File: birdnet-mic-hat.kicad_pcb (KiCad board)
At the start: 4 copper layers, 17.8 x 22.7 mm, 26 parts, among them J1 PJ-327A0-SMT, J3 DF40HC(3.5)-30DS-0.4V(51), Q1 MMBT3904, U1 TLV320ADC5140, U2 TPS7A2033PDBVR

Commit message: Remove manually placed C12 and J1 silkscreen labels
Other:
- board text removed: "C12"
- board text removed: "J1"

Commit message: Remove remaining MIC and MIC HAT silkscreen text
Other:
- board text removed: "MIC"
- board text removed: "MIC HAT"
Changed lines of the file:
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@@
 		(layer "Edge.Cuts")
-	)
-	(gr_text "MIC"
-		(at 102.3 107.98 0)
-		(layer "F.SilkS")
-		(effects
-			(font
-				(size 0.8 0.8)
-				(thickness 0.12)
-			)
-		)
-	)
-	(gr_text "MIC HAT"
-		(at 100.8 125.4 90)
-		(layer "F.SilkS")
-		(effects
-			(font
-				(size 0.8 0.8)
-				(thickness 0.12)
-			)
-		)
 	)
 	(segment

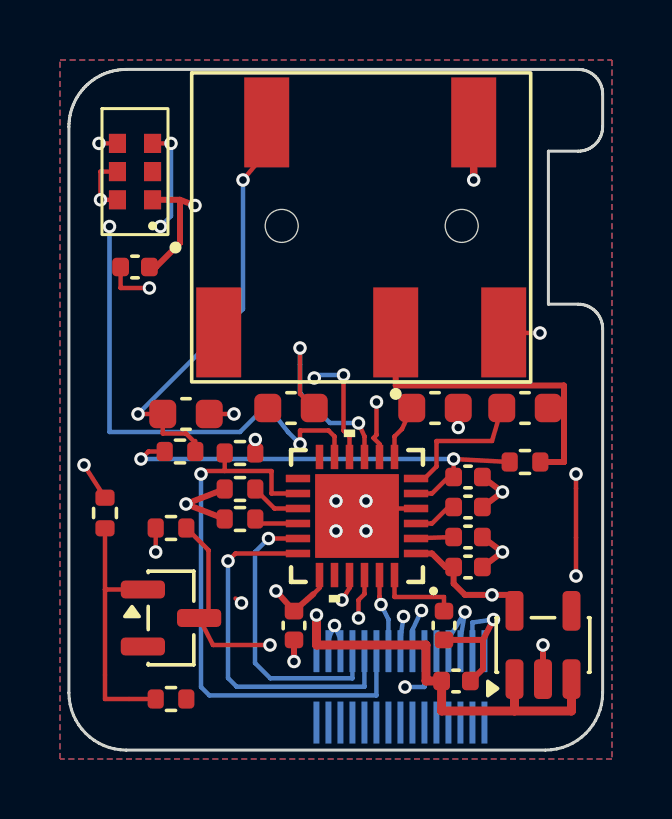
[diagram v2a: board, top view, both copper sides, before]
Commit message: Save manual routing refinements before trace cleanup
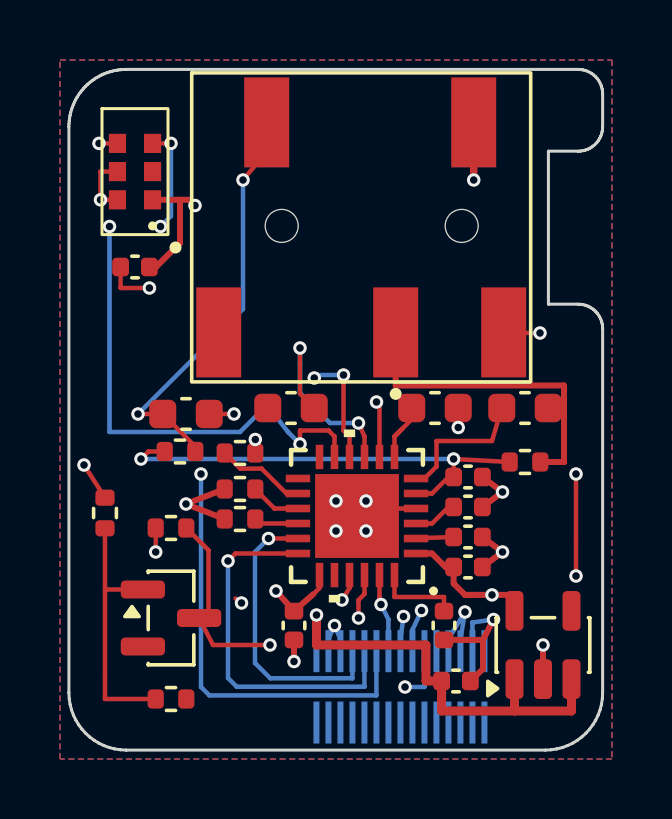
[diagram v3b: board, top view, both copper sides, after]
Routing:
- net /ADC_RST: track 18.7 -> 17.4 mm
- net /JACK_RING: track 13.1 -> 12.6 mm
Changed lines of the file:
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@@
-	)
-	(segment
-		(start 104 119.35)
-		(end 104.31 119.66)
-		(width 0.15)
-		(layer "F.Cu")
-		(net "/JACK_RING")
 	)
 	(segment
 		(start 104.31 119.95)
-		(end 104.31 119.6)
+		(end 104.31 119.785)
 		(width 0.15)
 		(layer "F.Cu")
@@
 	(segment
 		(start 103.225 118.7)
-		(end 103.225 119.35)
+		(end 102.4 118.7)
 		(width 0.15)
 		(layer "F.Cu")
@@
 	)
 	(segment
-		(start 103.225 118.7)
-		(end 102.4 118.7)
-		(width 0.15)
-		(layer "F.Cu")
-		(net "/JACK_RING")
-	)
-	(segment
-		(start 103.225 119.35)
-		(end 104 119.35)
+		(start 104.31 119.785)
+		(end 103.225 118.7)
 		(width 0.15)
 		(layer "F.Cu")
@@
 	)
 	(segment
-		(start 106.85 121.35)
-		(end 106.85 120.6)
+		(start 105.811999 120.522)
+		(end 105.289999 120)
+		(width 0.15)
+		(layer "F.Cu")
+		(net "/ADC_RST")
+	)
+	(segment
+		(start 107.7315 121.349999)
+		(end 107.349999 121.349999)
 		(width 0.15)
 		(layer "F.Cu")
@@
 	)
 	(segment
-		(start 105.29 120.6)
-		(end 105.29 120)
+		(start 106.522 120.522)
+		(end 105.811999 120.522)
 		(width 0.15)
 		(layer "F.Cu")
@@
 	)
 	(segment
-		(start 107.531 121.35)
-		(end 106.85 121.35)
-		(width 0.15)
-		(layer "F.Cu")
-		(net "/ADC_RST")
-	)
-	(segment
-		(start 106.85 120.6)
-		(end 104.6 120.6)
+		(start 107.349999 121.349999)
+		(end 106.522 120.522)
 		(width 0.15)
 		(layer "F.Cu")
@@
 	)
 	(segment
-		(start 103.8 111.56)
-		(end 104.3 111.75)
-		(width 0.2)
-		(layer "F.Cu")
-		(net "AVDD")
-	)
-	(segment
 		(start 103.8 113)
 		(end 103 113.8)
@@
 	)
 	(segment
+		(start 104.11 111.56)
+		(end 104.3 111.75)
+		(width 0.2)
+		(layer "F.Cu")
+		(net "AVDD")
+	)
+	(segment
+		(start 103.8 111.56)
+		(end 104.11 111.56)
+		(width 0.2)
+		(layer "F.Cu")
+		(net "AVDD")
+	)
+	(segment
 		(start 112.2 123.35)
 		(end 112.65 123.8)
@@
 	(segment
 		(start 115.3 113.5)
+		(end 115.3 123.63)
+		(width 0.2)
+		(layer "In2.Cu")
+		(net "AVDD")
+	)
+	(segment
+		(start 115.3 123.63)
+		(end 114.2 124.73)
+		(width 0.2)
+		(layer "In2.Cu")
+		(net "AVDD")
+	)
+	(segment
+		(start 104.3 111.75)
 		(end 104.3 113.5)
 		(width 0.2)
@@
 	)
 	(segment
-		(start 114.2 124.73)
-		(end 115.3 123.63)
-		(width 0.2)
-		(layer "In2.Cu")
-		(net "AVDD")
-	)
-	(segment
-		(start 115.3 123.63)
+		(start 104.3 113.5)
 		(end 115.3 113.5)
-		(width 0.2)
-		(layer "In2.Cu")
-		(net "AVDD")
-	)
-	(segment
-		(start 104.3 113.5)
-		(end 104.3 111.75)
 		(width 0.2)
 		(layer "In2.Cu")
@@
 	)
 	(segment
-		(start 110.35 118.3)
-		(end 110.35 119.4)
+		(start 110.450001 120.1315)
+		(end 110.450001 118.400001)
 		(width 0.15)
 		(layer "F.Cu")
@@
 	)
 	(segment
-		(start 110.25 119.5)
-		(end 110.45 119.7)
-		(width 0.15)
-		(layer "F.Cu")
-		(net "/MIC_RING")
-	)
-	(segment
-		(start 110.35 119.4)
-		(end 110.25 119.5)
-		(width 0.15)
-		(layer "F.Cu")
-		(net "/MIC_RING")
-	)
-	(segment
-		(start 110.45 119.7)
-		(end 110.45 120.1315)
+		(start 110.450001 118.400001)
+		(end 110.35 118.3)
 		(width 0.15)
 		(layer "F.Cu")
@@
 	)
 	(segment
-		(start 111.2 119.2)
-		(end 111.525 118.5)
+		(start 111.524999 118.875001)
+		(end 111.524999 118.5)
 		(width 0.15)
 		(layer "F.Cu")
@@
 		(width 0.15)
 		(layer "F.Cu")
+		(net "/MIC_TIP_N")
+	)
+	(segment
+		(start 110.95 119.45)
+		(end 111.524999 118.875001)
+		(width 0.15)
+		(layer "F.Cu")

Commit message: Clean supply and signal routing and remove redundant via
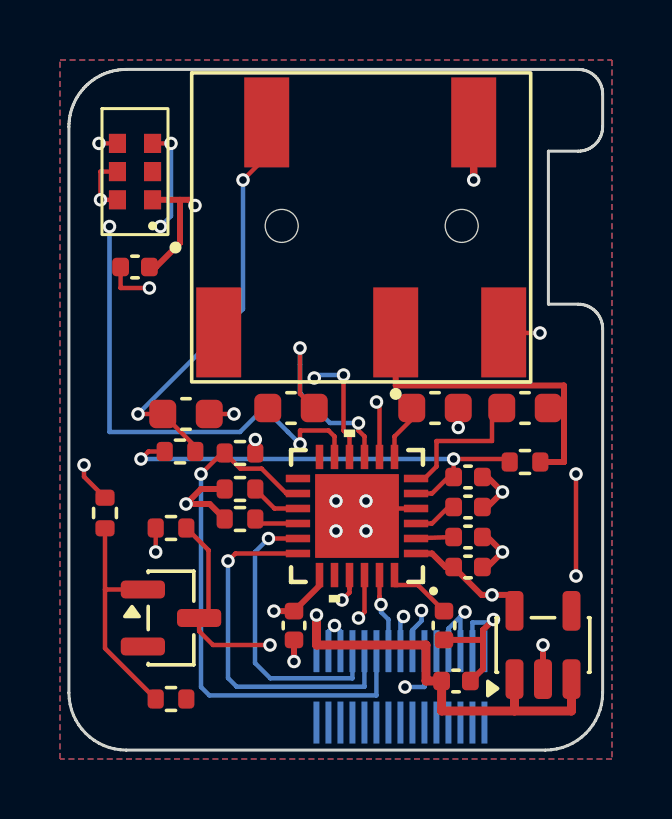
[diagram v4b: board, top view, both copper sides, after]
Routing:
- net AVDD: track 33.6 -> 32.5 mm
- net Net-(Q1-B): track 8.64 -> 7.65 mm
- net /ADC_RST: track 17.4 -> 18.3 mm
- net GND: track 20.9 -> 21.5 mm
- net DREG: track 2.85 -> 2.34 mm
- net VCC_3V3: track 23.5 -> 23.3 mm, vias 5 -> 4

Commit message: Route PDM signals on front copper and remove seven signal vias
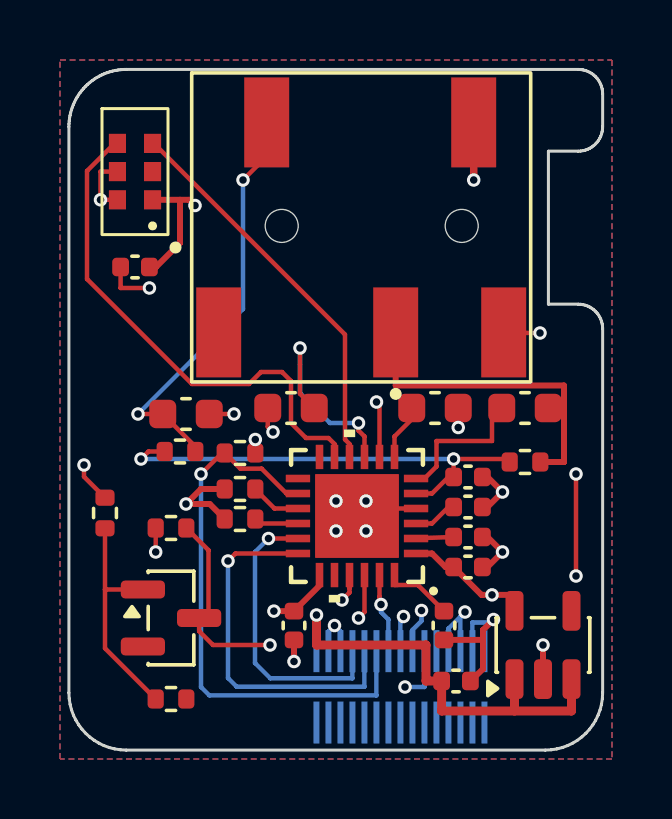
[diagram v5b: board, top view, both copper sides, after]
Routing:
- net /PDM_CLK: track 20.4 -> 17.1 mm, vias 3 -> 0
- net /PDM_DATA: track 16.0 -> 13.2 mm, vias 4 -> 0
- net GND: track 21.5 -> 22.3 mm, vias 15 -> 16
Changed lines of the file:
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@@
+	)
+	(segment
+		(start 106.725 119.125)
+		(end 106.9 119.3)
+		(width 0.15)
+		(layer "F.Cu")
+		(net "GND")
 	)
 	(segment
@@
 	)
 	(segment
+		(start 106.725 118.5)
+		(end 106.725 119.125)
+		(width 0.15)
+		(layer "F.Cu")
+		(net "GND")
+	)
+	(segment
 		(start 113.88 122.8)
 		(end 114.05 122.8)
@@
 	)
 	(via
+		(at 106.9 119.3)
+		(size 0.45)
+		(drill 0.25)
+		(layers "F.Cu" "B.Cu")
+		(net "GND")
+	)
+	(via
 		(at 110 121.6)
 		(size 0.45)
@@
 	)
 	(segment
-		(start 109.25 117.4)
-		(end 109.25 119.25)
+		(start 102.884999 109.68)
+		(end 102.93 109.68)
 		(width 0.15)
 		(layer "F.Cu")
@@
 	)
 	(segment
-		(start 109.45 119.45)
+		(start 109.3 119.55)
+		(end 109.45 119.7)
+		(width 0.15)
+		(layer "F.Cu")
+		(net "/PDM_DATA")
+	)
+	(segment
+		(start 102.93 109.68)
+		(end 109.3 116.05)
+		(width 0.15)
+		(layer "F.Cu")
+		(net "/PDM_DATA")
+	)
+	(segment
+		(start 109.3 116.05)
+		(end 109.3 119.55)
+		(width 0.15)
+		(layer "F.Cu")
+		(net "/PDM_DATA")
+	)
+	(segment
+		(start 109.45 119.7)
 		(end 109.45 120.1315)
 		(width 0.15)
@@
 	)
 	(segment
-		(start 109.25 119.25)
-		(end 109.45 119.45)
-		(width 0.15)
-		(layer "F.Cu")
-		(net "/PDM_DATA")
-	)
-	(segment
-		(start 102.885 109.68)
-		(end 103.5 109.68)
-		(width 0.15)
-		(layer "F.Cu")
-		(net "/PDM_DATA")
-	)
-	(via
-		(at 103.15 112.45)
-		(size 0.45)
-		(drill 0.25)
-		(layers "F.Cu" "B.Cu")
-		(net "/PDM_DATA")
-	)
-	(via
-		(at 108.275 117.5)
-		(size 0.45)
-		(drill 0.25)
-		(layers "F.Cu" "B.Cu")
-		(net "/PDM_DATA")
-	)
-	(via
-		(at 109.25 117.4)
-		(size 0.45)
-		(drill 0.25)
-		(layers "F.Cu" "B.Cu")
-		(net "/PDM_DATA")
-	)
-	(via
-		(at 103.5 109.68)
-		(size 0.45)
-		(drill 0.25)
-		(layers "F.Cu" "B.Cu")
-		(net "/PDM_DATA")
-	)
-	(segment
-		(start 108.375 117.4)
-		(end 109.25 117.4)
-		(width 0.15)
-		(layer "B.Cu")
-		(net "/PDM_DATA")
-	)
-	(segment
-		(start 103.5 109.68)
-		(end 103.5 112.1)
-		(width 0.15)
-		(layer "B.Cu")
-		(net "/PDM_DATA")
-	)
-	(segment
-		(start 103.5 112.1)
-		(end 103.15 112.45)
-		(width 0.15)
-		(layer "B.Cu")
-		(net "/PDM_DATA")
-	)
-	(segment
-		(start 108.275 117.5)
-		(end 108.375 117.4)
-		(width 0.15)
-		(layer "B.Cu")
-		(net "/PDM_DATA")
-	)
-	(segment
-		(start 105.7 117.4)
-		(end 108.175 117.4)
-		(width 0.15)
-		(layer "In2.Cu")
-		(net "/PDM_DATA")
-	)
-	(segment
-		(start 103.5 115.2)
-		(end 105.7 117.4)
-		(width 0.15)
-		(layer "In2.Cu")
-		(net "/PDM_DATA")
-	)
-	(segment
-		(start 103.15 112.45)
-		(end 103.5 112.8)
-		(width 0.15)
-		(layer "In2.Cu")
-		(net "/PDM_DATA")
-	)
-	(segment
-		(start 108.175 117.4)
-		(end 108.275 117.5)
-		(width 0.15)
-		(layer "In2.Cu")
-		(net "/PDM_DATA")
-	)
-	(segment
-		(start 103.5 112.8)
-		(end 103.5 115.2)
-		(width 0.15)
-		(layer "In2.Cu")
-		(net "/PDM_DATA")
+		(start 104.2 117.7)
+		(end 106.1 117.7)
+		(width 0.15)
+		(layer "F.Cu")
+		(net "/PDM_CLK")
+	)
+	(segment
+		(start 100.7 114.2)
+		(end 104.2 117.7)
+		(width 0.15)
+		(layer "F.Cu")
+		(net "/PDM_CLK")
+	)
+	(segment
+		(start 106.1 117.7)
+		(end 106.5 117.3)
+		(width 0.15)
+		(layer "F.Cu")
+		(net "/PDM_CLK")
+	)
+	(segment
+		(start 106.5 117.3)
+		(end 107.2 117.3)
+		(width 0.15)
+		(layer "F.Cu")
+		(net "/PDM_CLK")
+	)
+	(segment
+		(start 108.95 119.7)
+		(end 108.95 120.1315)
+		(width 0.15)
+		(layer "F.Cu")
+		(net "/PDM_CLK")
+	)
+	(segment
+		(start 107.5 117.6)
+		(end 107.5 119)
+		(width 0.15)
+		(layer "F.Cu")
+		(net "/PDM_CLK")
+	)
+	(segment
+		(start 108 119.5)
+		(end 108.75 119.5)
+		(width 0.15)
+		(layer "F.Cu")
+		(net "/PDM_CLK")
+	)
+	(segment
+		(start 101.62 109.68)
+		(end 100.7 110.6)
+		(width 0.15)
+		(layer "F.Cu")
+		(net "/PDM_CLK")
+	)
+	(segment
+		(start 107.2 117.3)
+		(end 107.5 117.6)
+		(width 0.15)
+		(layer "F.Cu")
+		(net "/PDM_CLK")
+	)
+	(segment
+		(start 108.75 119.5)
+		(end 108.95 119.7)
+		(width 0.15)
+		(layer "F.Cu")
+		(net "/PDM_CLK")
 	)
 	(segment
 		(start 101.715 109.68)
-		(end 101.1 109.68)
-		(width 0.15)
-		(layer "F.Cu")
-		(net "/PDM_CLK")
-	)
-	(segment
-		(start 107.8 119.25)
-		(end 108.75 119.25)
-		(width 0.15)
-		(layer "F.Cu")
-		(net "/PDM_CLK")
-	)
-	(segment
-		(start 108.75 119.25)
-		(end 108.95 119.45)
-		(width 0.15)
-		(layer "F.Cu")
-		(net "/PDM_CLK")
-	)
-	(segment
-		(start 107.8 119.7)
-		(end 107.8 119.25)
-		(width 0.15)
-		(layer "F.Cu")
-		(net "/PDM_CLK")
-	)
-	(segment
-		(start 108.95 119.45)
-		(end 108.95 120.1315)
-		(width 0.15)
-		(layer "F.Cu")
-		(net "/PDM_CLK")
-	)
-	(via
-		(at 101.1 109.68)
-		(size 0.45)
-		(drill 0.25)
-		(layers "F.Cu" "B.Cu")
-		(net "/PDM_CLK")
-	)
-	(via
-		(at 101.45 112.45)
-		(size 0.45)
-		(drill 0.25)
-		(layers "F.Cu" "B.Cu")
-		(net "/PDM_CLK")
-	)
-	(via
-		(at 107.8 119.7)
-		(size 0.45)
-		(drill 0.25)
-		(layers "F.Cu" "B.Cu")
-		(net "/PDM_CLK")
-	)
-	(segment
-		(start 107.4 119.3)
-		(end 107.8 119.7)
-		(width 0.15)
-		(layer "B.Cu")
-		(net "/PDM_CLK")
-	)
-	(segment
-		(start 101.45 119.3)
-		(end 105.8 119.3)
-		(width 0.15)
-		(layer "B.Cu")
-		(net "/PDM_CLK")
-	)
-	(segment
-		(start 106.7 118.6)
-		(end 107.4 119.3)
-		(width 0.15)
-		(layer "B.Cu")
-		(net "/PDM_CLK")
-	)
-	(segment
-		(start 105.8 119.3)
-		(end 106.7 118.4)
-		(width 0.15)
-		(layer "B.Cu")
-		(net "/PDM_CLK")
-	)
-	(segment
-		(start 106.7 118.4)
-		(end 106.7 118.6)
-		(width 0.15)
-		(layer "B.Cu")
-		(net "/PDM_CLK")
-	)
-	(segment
-		(start 101.45 112.45)
-		(end 101.45 119.3)
-		(width 0.15)
-		(layer "B.Cu")
-		(net "/PDM_CLK")
-	)
-	(segment
-		(start 101.8 110.38)
-		(end 101.8 112.1)
-		(width 0.15)
-		(layer "In2.Cu")
-		(net "/PDM_CLK")
-	)
-	(segment
-		(start 101.8 112.1)
-		(end 101.45 112.45)
-		(width 0.15)
-		(layer "In2.Cu")
-		(net "/PDM_CLK")
-	)
-	(segment
-		(start 101.1 109.68)
-		(end 101.8 110.38)
-		(width 0.15)
-		(layer "In2.Cu")
-		(net "/PDM_CLK")
-	)
+		(end 101.62 109.68)
+		(width 0.15)
+		(layer "F.Cu")
+		(net "/PDM_CLK")
+	)
+	(segment
+		(start 100.7 110.6)
+		(end 100.7 114.2)
+		(width 0.15)
+		(layer "F.Cu")
+		(net "/PDM_CLK")
+	)
+	(segment
+		(start 107.5 119)
+		(end 108 119.5)
+		(width 0.15)
+		(layer "F.Cu")
+		(net "/PDM_CLK")
+	)
